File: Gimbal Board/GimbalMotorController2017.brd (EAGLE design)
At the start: 83.4 x 79.2 mm, 125 parts, among them J1 SL03THROUGH_HOLE, J3 APP_2POS_CONFIG5V_HORIZ, Q7 MOSFET-PCHANNEL, Q8 MOSFET-PCHANNEL, Q9 MOSFET-NCHANNELAO3404A, U1 NUP4201MR6, U2 MAX3232D, U3 CSD18533Q5A, U4 CSD18533Q5A, U5 CSD18533Q5A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

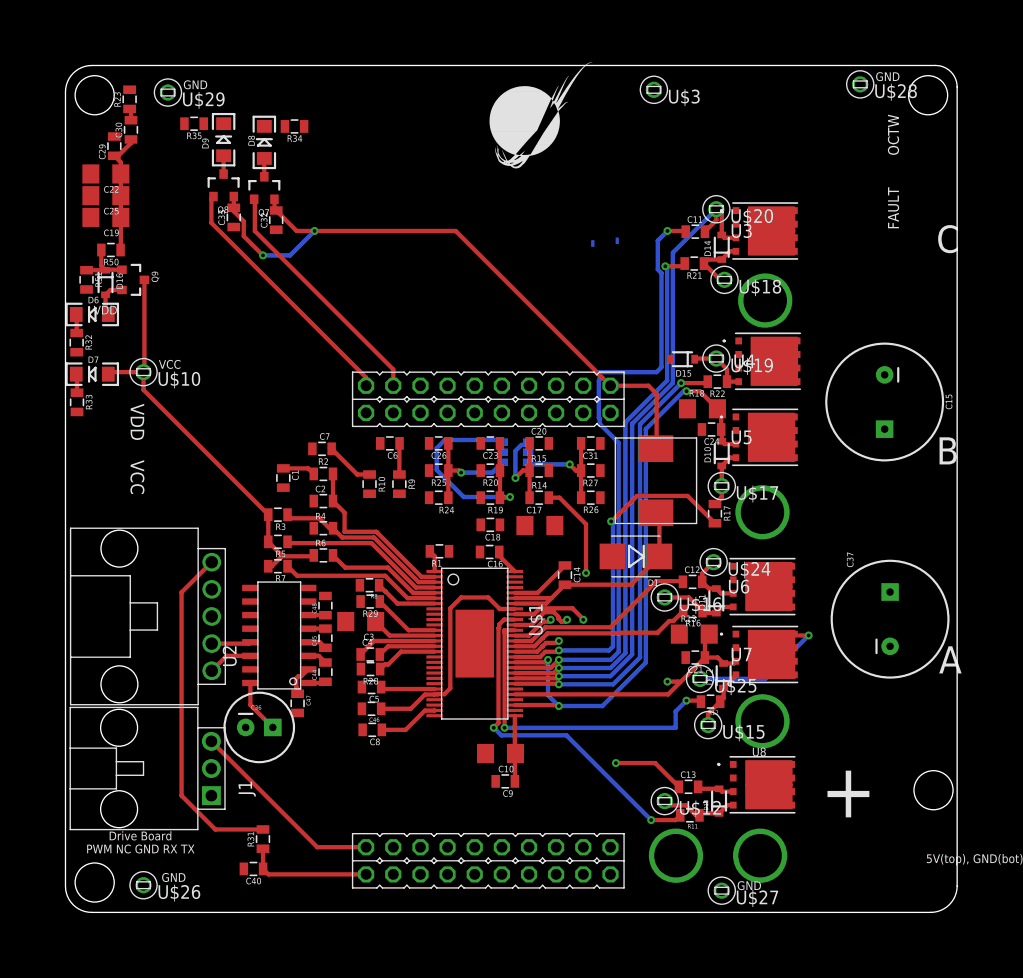
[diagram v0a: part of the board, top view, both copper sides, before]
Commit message: Finished Tracing
All clearance issues have been fixed. The board's tracing issues have been fixed. All overlap issues have been fixed. It is now ready for Board Review.
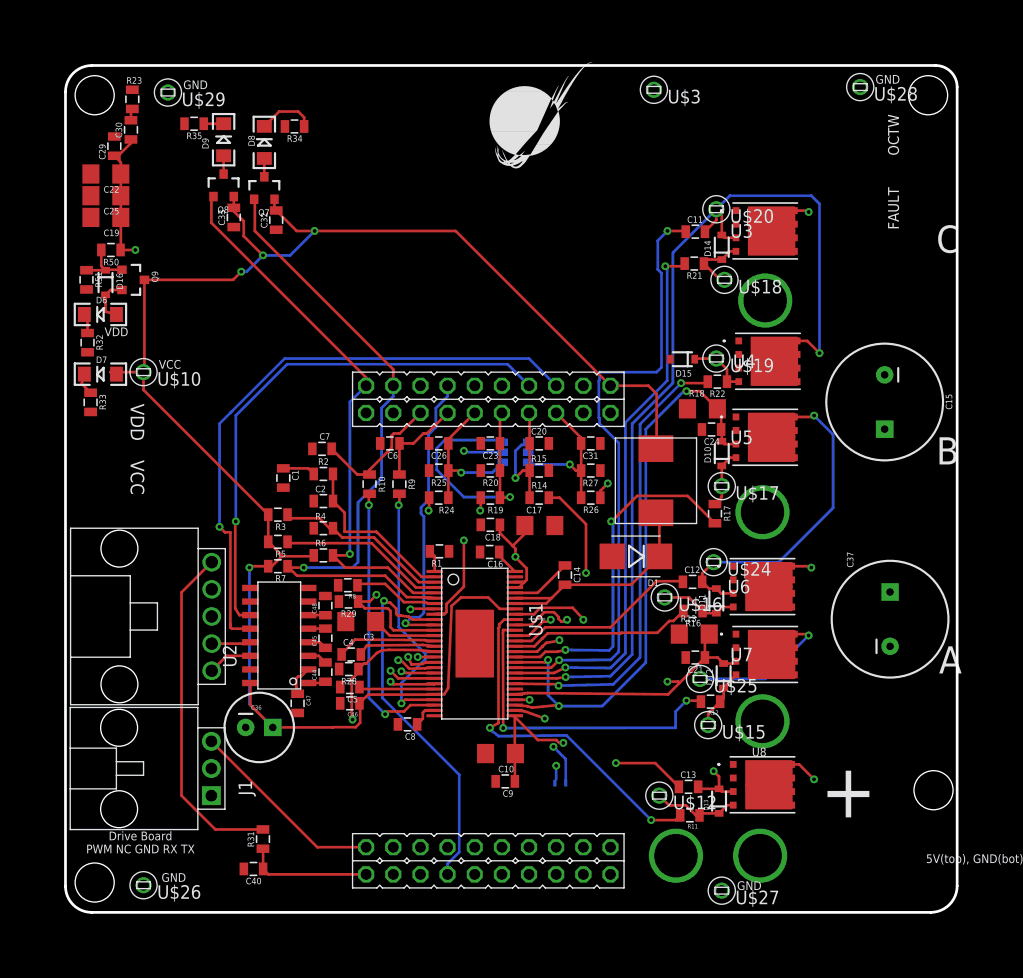
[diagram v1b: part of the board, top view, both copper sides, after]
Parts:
- moved SH1 51.0 mm to (59.3, 12.4), turned to 90 degrees
- moved SH2 50.6 mm to (58.3, 12.4), turned to 90 degrees
- moved C8 3.34 mm to (44.5, 17.8)
- moved C46 2.09 mm to (39.1, 19.8)
- moved C5 2.03 mm to (39.1, 21.3)
- moved R28 2.03 mm to (39.0, 23.0)
- moved R29 2.03 mm to (39.0, 29.3)
- moved R8 2.03 mm to (38.9, 30.9)
- moved C4 1.78 mm to (39.2, 24.4)
- moved R33 1.27 mm to (14.9, 48.0)
- moved R32 1.02 mm to (14.6, 53.6)
- moved D6 0.76 mm to (15.8, 56.2)
- moved D7 0.76 mm to (15.8, 50.6)
- moved U$12 0.72 mm to (68.1, 11.2)
- moved U$28 0.25 mm to (86.9, 77.5)
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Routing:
- net VCC: track 127.1 -> 190.2 mm, vias 2 -> 5
- net UART_RX: track 0.00 -> 57.2 mm, vias 0 -> 1
- net UART_TX: track 0.00 -> 50.1 mm, vias 0 -> 1
- net SDI: track 0.00 -> 49.7 mm, vias 0 -> 1
- net SH_C: track 63.4 -> 113.1 mm, vias 1 -> 3
- net PVDD: track 17.5 -> 62.4 mm, vias 0 -> 7
- net NSCS: track 0.00 -> 42.7 mm, vias 0 -> 1
- net SH_B: track 27.9 -> 68.8 mm, vias 1 -> 3
- net DC_CAL: track 6.24 -> 44.2 mm, vias 0 -> 1
- net SDO: track 0.00 -> 34.8 mm, vias 0 -> 1
- net EN_GATE: track 5.77 -> 37.0 mm, vias 0 -> 1
- net INL_A: track 0.00 -> 27.8 mm, vias 0 -> 1
- net SCLK: track 0.00 -> 27.6 mm, vias 0 -> 1
- net INH_A: track 0.00 -> 27.6 mm, vias 0 -> 1
- net INH_B: track 0.00 -> 27.4 mm, vias 0 -> 1
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- added copper zone on layer 2, net SH_A
- added copper zone on layer 2, net SH_B
- added copper zone on layer 2, net SH_C

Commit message: Shrank Board
Board is now smaller
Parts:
- moved U$3 17.4 mm to (51.8, 69.8)
- moved C19 13.0 mm to (27.0, 57.9)
- moved C29 13.0 mm to (27.7, 64.6)
- moved C33 13.0 mm to (38.9, 57.9)
- moved D8 13.0 mm to (41.8, 64.9)
- moved R32 13.0 mm to (25.2, 46.2)
- moved R33 13.0 mm to (25.5, 40.6)
- moved R51 13.0 mm to (25.1, 52.1)
- moved C22 13.0 mm to (27.0, 62.0)
- moved C25 13.0 mm to (27.0, 59.9)
- moved C30 13.0 mm to (29.3, 66.1)
- moved C32 13.0 mm to (42.9, 57.7)
- moved D16 13.0 mm to (26.9, 51.8)
- moved D6 13.0 mm to (26.4, 48.8)
- moved D7 13.0 mm to (26.4, 43.2)
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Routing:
- net VCC: track 190.2 -> 164.4 mm
- net NOCTW: track 52.7 -> 40.3 mm
- net NFAULT: track 62.5 -> 50.2 mm
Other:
- board size 83.4 x 79.2 mm -> 83.4 x 72.1 mm

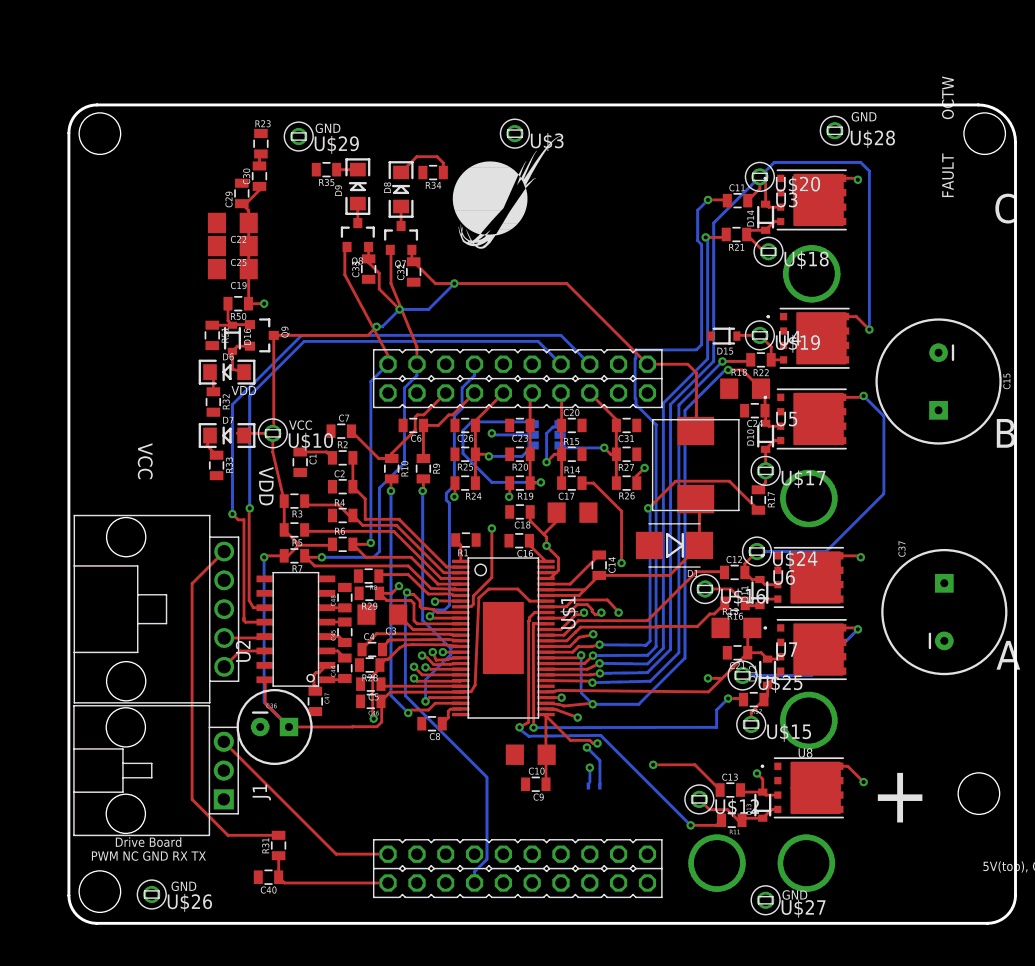
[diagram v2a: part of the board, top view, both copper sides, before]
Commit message: Smashed and Via Patched the Board
Almost every surface mount now has a via connecting it to the other three ground plains. Silkscreen is a WIP.
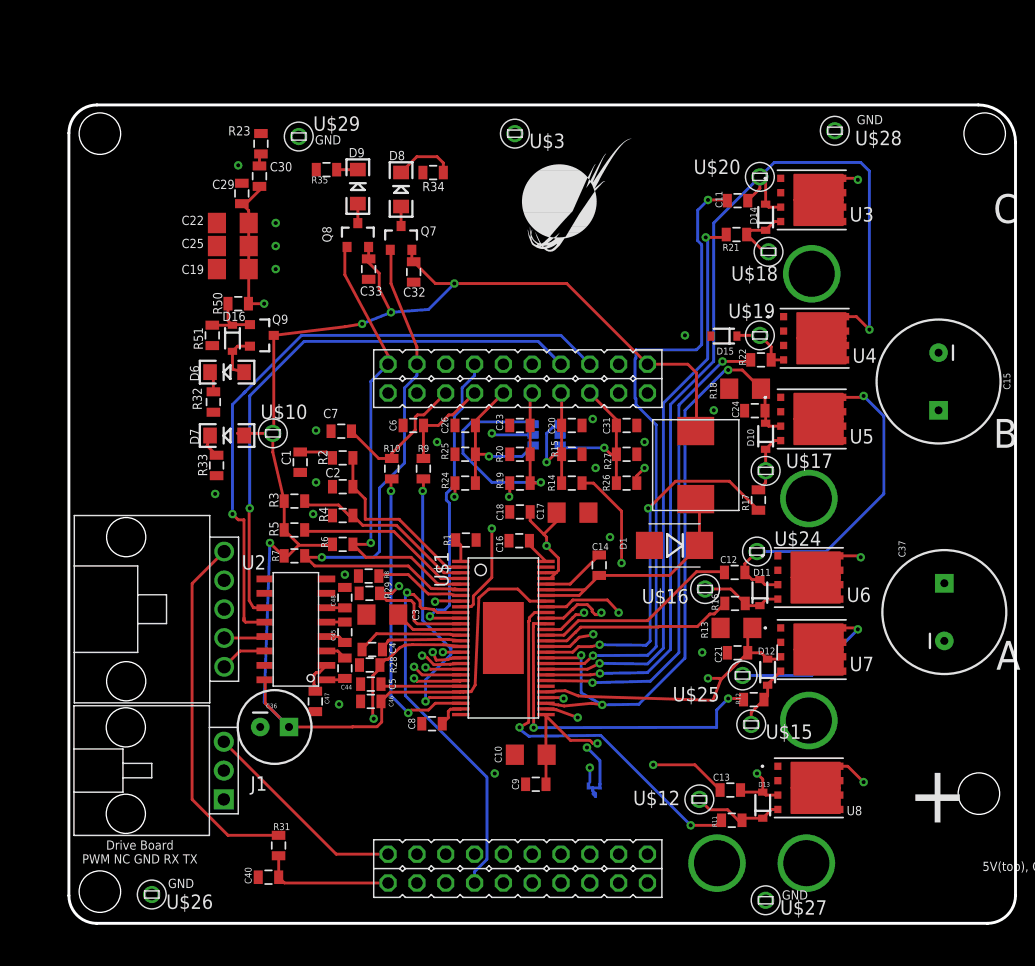
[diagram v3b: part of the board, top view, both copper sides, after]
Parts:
- moved U$9 6.10 mm to (52.4, 58.6)
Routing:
- net GND: track 0.00 -> 2.25 mm, vias 0 -> 19
- net SL_A: track 49.7 -> 50.6 mm
- net SL_B: track 57.3 -> 58.0 mm
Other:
- board text removed: "FAULT"
- board text removed: "OCTW"
- board text removed: "VCC"
- board text removed: "VDD"
